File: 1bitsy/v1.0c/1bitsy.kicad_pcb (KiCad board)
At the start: 4 copper layers, 38.1 x 17.8 mm, 99 parts, among them J1 BOOT, P1 CONN_01X01, P10 CONN_01X01, P11 CONN_01X01, P12 CONN_01X01, P13 CONN_01X01, P14 CONN_01X01, P15 CONN_01X01, P16 CONN_01X01, P17 CONN_01X01, P18 CONN_01X01, P19 CONN_01X01, P2 CONN_01X01, P20 CONN_01X01, P21 CONN_01X01, P22 CONN_01X01, P23 CONN_01X01, P24 USB_OTG, P25 CONN_01X01, P26 CONN_01X01, P27 CONN_01X01, P28 CONN_01X01, P29 CONN_01X01, P3 CONN_01X01, P30 CONN_01X01, P31 CONN_01X01, P32 CONN_01X01, P33 CONN_01X01, P34 CONN_01X01, P35 CONN_01X01, P36 CONN_01X01, P37 CONN_01X01, P38 CONN_01X01, P39 CONN_01X01, P4 CONN_01X01, P40 CONN_01X01, P41 CONN_01X01, P42 CONN_01X01, P43 TP, P44 TP, P45 TP, P46 TP, P47 TP, P48 CONN_01X01, P49 CONN_01X01, P5 CONN_01X01, P50 CONN_01X01, P51 CONN_01X01, P52 CONN_01X01, P53 CONN_01X01, P54 CONN_01X01, P55 CONN_01X01, P6 CONN_01X01, P7 CONN_01X01, P8 CONN_01X01, P9 CONN_01X01, SW1 TACT_G, U1 VREG_3V3, U2 STM32F415RGT, X1 32.768kHz, X2 25MHz, X3 JTAG-10

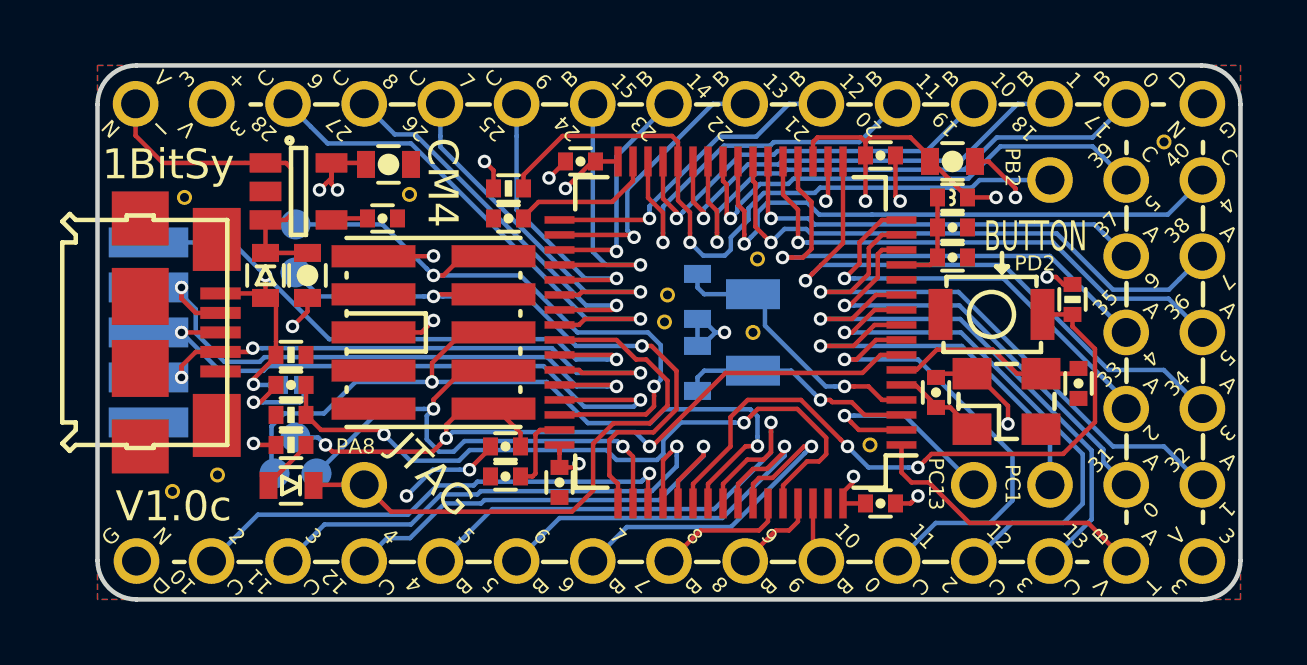
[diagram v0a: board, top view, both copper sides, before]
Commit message: Exposed the PD2 pin to allow 4pin SDIO.
The PD2 pin was connected to the button making 4bit SDIO difficult to
implement. This resulted in a bunch of IO pins changing their positions:
* Button: PD2 -> PC1
*  5: PB4 -> PD2
*  6: PB5 -> PB4
*  7: PB6 -> PB5
*  8: PB7 -> PB6
*  9: PB8 -> PB7
* 10: PB9 -> PB8
* 11: PC0 -> PB9
* XX: PC1 -> PC0
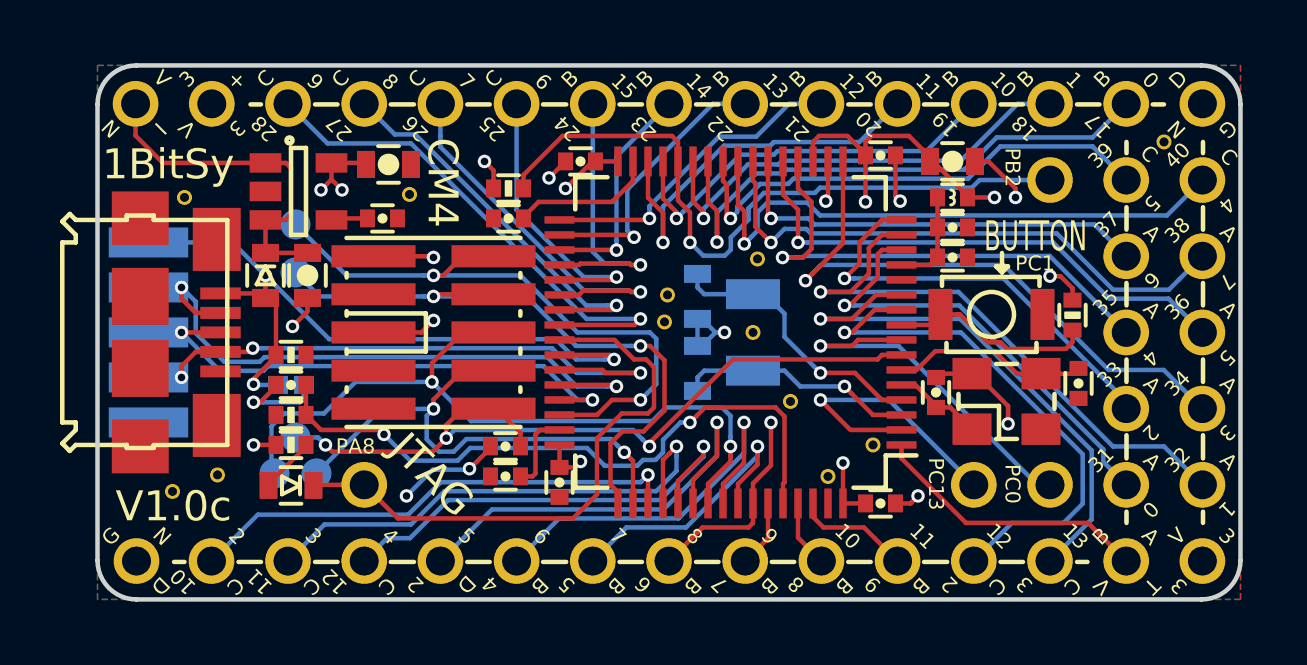
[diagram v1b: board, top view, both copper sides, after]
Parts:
- added REF**: via0305, pkl_misc:via0305, F.Cu at (123.4, 48.0)
- added REF**: via0305, pkl_misc:via0305, F.Cu at (124.7, 50.5)
- L1: value Ferr -> 600 Ferrite
- moved P11 20.5 mm to (111.8, 53.3)
- moved P10 5.68 mm to (132.1, 50.8)
- moved P29 2.54 mm to (116.8, 53.3)
- moved P31 2.54 mm to (121.9, 53.3)
- moved P33 2.54 mm to (127.0, 53.3)
- moved P28 2.54 mm to (114.3, 53.3)
- moved P30 2.54 mm to (119.4, 53.3)
- moved P32 2.54 mm to (124.5, 53.3)
- moved R5 0.52 mm to (132.8, 45.1)
- moved REF** 0.10 mm to (126.2, 49.5)
- turned SW1 to 270 degrees
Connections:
- P11 pad 1: /PC1 -> /PD2
- U2 pad 54: /BUTTON -> /PD2
- U2 pad 9: /PC1 -> /BUTTON
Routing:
- net /BUTTON: track 22.2 -> 6.81 mm, vias 2 -> 0
- net /PD2: track 0.00 -> 14.8 mm, vias 0 -> 1
- net /PC1: track 13.5 -> 0.00 mm, vias 1 -> 0
- net /PB6: track 12.0 -> 6.95 mm
- net /PB4: track 17.2 -> 13.1 mm
- net /PB5: track 13.5 -> 9.43 mm
- net /USB_D+: track 20.5 -> 17.2 mm
- net /PC0: track 15.3 -> 12.4 mm
- net /PB7: track 4.45 -> 2.23 mm
- net /PC13: track 7.36 -> 9.40 mm
- net /PB9: track 2.04 -> 3.88 mm
- net /BOOT0: track 23.6 -> 22.1 mm
- net /JTAG_TDO: track 26.2 -> 24.7 mm
- net /JTAG_TCK: track 22.3 -> 21.6 mm
- net /PB8: track 2.91 -> 2.24 mm
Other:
- board text added: "PC0"
- board text removed: "PD2"

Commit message: Changed the boot jumper to 0603 size.
This should make manual soldering of it slightly easier.
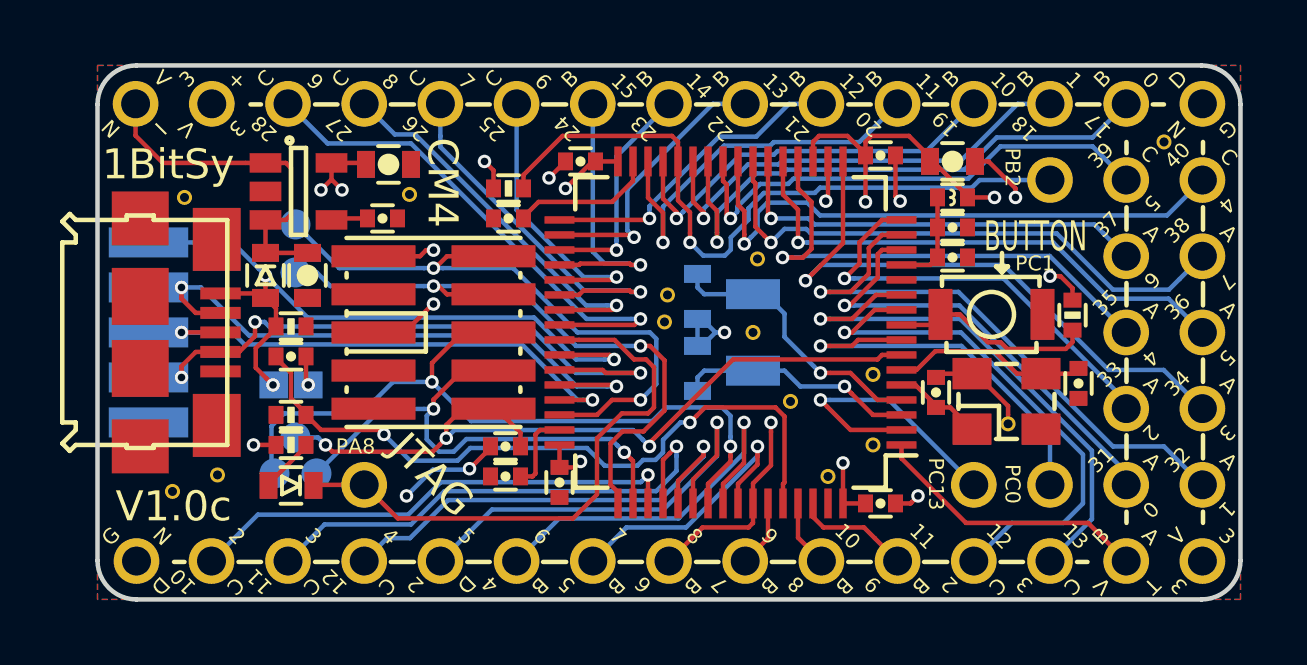
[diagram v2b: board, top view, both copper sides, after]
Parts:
- added REF**: via0305, pkl_misc:via0305, F.Cu at (130.7, 48.8)
- added REF**: via0305, pkl_misc:via0305, F.Cu at (126.2, 47.1)
- J1: footprint pkl_jumpers:J_0402 -> pkl_jumpers:J_0603
- moved C15 0.95 mm to (106.8, 46.5), turned to 180 degrees
- moved R1 0.95 mm to (106.8, 45.5)
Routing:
- net Net-(C15-Pad1): track 3.20 -> 0.98 mm
- net /BOOT0: track 22.1 -> 23.5 mm
- net /USB_ID: track 19.0 -> 20.0 mm
- net /PC0: track 12.4 -> 13.3 mm
- net GND: track 21.8 -> 20.8 mm, vias 12 -> 10
- net /USB_D-: track 20.4 -> 19.7 mm
- net /USB_VBUS: track 25.6 -> 24.9 mm
